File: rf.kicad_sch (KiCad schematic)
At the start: 10 parts, among them Q1 2N7002

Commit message: finish up everything but nfc
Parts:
- added U11: SN74AUP1G17, Package_TO_SOT_SMD:Diodes_SOT-553, symbol 74xGxx:74LVC1G17
- added U13: ST25R3916B-AQET, ST25R3916B-AQET:QFN-32_L5.0-W5.0-P0.50-TL-EP3.5, symbol ST25R3916B-AQET:ST25R3916B-AQET
- C33: LCSC Part (none) -> C1538
- C34: footprint (none) -> Capacitor_SMD:C_0402_1005Metric; LCSC Part (none) -> C15195
- L5: footprint (none) -> custom_footprints:Generic_Solder_Pads_2P; now left out of the parts list
- Q1: LCSC Part (none) -> C8545
- R41: footprint (none) -> Resistor_SMD:R_0402_1005Metric; LCSC Part (none) -> C25744
- R42: footprint (none) -> Resistor_SMD:R_0402_1005Metric; LCSC Part (none) -> C25741
- R43: footprint (none) -> Resistor_SMD:R_0603_1608Metric; LCSC Part (none) -> C21190
- R44: footprint (none) -> Resistor_SMD:R_0402_1005Metric; LCSC Part (none) -> C25792
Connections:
- net GND: now also U11.3 (GND)
- net RF_WAKE: now also U11.4; no longer D3.1 (K), R44.2
- net RF_MOD renamed RF_DAT
- new net: D3.1 (K), R44.2, U11.2
- new net +3V3: U11.5 (VCC)
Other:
- moved on the sheet: C33, C34, D2, L5, Q1, R41, R42, R43, R44

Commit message: progress
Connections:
- net +3V3: now also U13.1 (VDD_IO)
- net GND: now also U13.12 (GND_DR), U13.16 (GND_DR)
- net NFC_CS: now reaches U13.29 (BSS)
- net NFC_CLK: now reaches U13.30 (SCLK/SCL)
- net NFC_DO: now reaches U13.31 (MOSI)
- net NFC_DI: now reaches U13.32 (MISO/SDA)
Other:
- moved on the sheet: U13

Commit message: push changes before removing fuel gauge
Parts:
- L5: now in the parts list
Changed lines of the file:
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@@
 		(unit 1)
 		(exclude_from_sim no)
-		(in_bom no)
+		(in_bom yes)
 		(on_board yes)
 		(dnp no)

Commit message: hopefully final schematic before splitting out
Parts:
- added C40, C41, C60: 10pF, Capacitor_SMD:C_0402_1005Metric, symbol Device:C_Small
- added C42, C46, C47, C49, C51, C53: 2.2uF, Capacitor_SMD:C_0402_1005Metric, symbol Device:C_Small
- added C43: 22nF, Capacitor_SMD:C_0402_1005Metric, symbol Device:C_Small
- added C44, C45, C48, C50, C52, C54, C56: 10nF, Capacitor_SMD:C_0402_1005Metric, symbol Device:C_Small
- added C55: 1uF, Capacitor_SMD:C_0402_1005Metric, symbol Device:C_Small
- added C57: 680pF, Capacitor_SMD:C_0402_1005Metric, symbol Device:C_Small
- added C58: 58pF, Capacitor_SMD:C_0402_1005Metric, symbol Device:C_Small
- added C59: 3pF, Capacitor_SMD:C_0402_1005Metric, symbol Device:C_Small
- added C61: 220pF, Capacitor_SMD:C_0402_1005Metric, symbol Device:C_Small
- added L7: 1462360151, custom_footprints:Generic_Solder_Pads_2P, symbol Device:L
- added L8: 270nH, Inductor_SMD:L_0603_1608Metric, symbol Device:L_Small
- added R24: 5.8, Resistor_SMD:R_0402_1005Metric, symbol Device:R_Small
- added TP14: NFC_CSO, TestPoint:TestPoint_Pad_D1.0mm, symbol Connector:TestPoint
- added TP15: NFC_CSI, TestPoint:TestPoint_Pad_D1.0mm, symbol Connector:TestPoint
- added Y3: 27.12MHz, Crystal:Crystal_SMD_2016-4Pin_2.0x1.6mm, symbol Device:Crystal_GND24_Small
- L6: renamed from L5; now left out of the parts list
- renumbered C33 to C38, C34 to C39, R41 to R20, R44 to R21, R42 to R22, R43 to R23, U11 to U12
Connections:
- net +3V3: now also U13.10 (VDD_TX), U13.8 (VDD), C44.1, C51.1, C52.1, C53.1, C54.1
- net GND: now also U13.20 (I2C_EN), U13.21 (VSS), U13.26 (GND_A), U13.33 (EP), U13.6 (GND_D), C40.2, C41.2, C42.2, C43.2, C44.2, C45.2, C46.2, C47.2, C48.2, C49.2, C50.2, C51.2, C52.2, C53.2, C54.2, C55.2, C56.2, C57.2, C59.2, C61.2, L7.2, Y3.2, Y3.4
- net VDD_AM: now reaches U13.11 (VDD_AM)
- net VDD_AM: now also C42.1, C43.1
- net RFO1: now reaches U13.13 (RFO1)
- net RFO1: now also L8.1
- net VDD_RF: now reaches U13.14 (VDD_DR)
- net VDD_RF: now also U13.9 (VDD_RF), C47.1, C48.1
- net at U13.2 (CSO): now also TP14.1
- net RFI1: now reaches U13.22 (RFI1)
- net RFI1: now also C60.1, C61.1
- net at U13.24 (AGDC): now also C55.1, C56.1
- net at U13.25 (CSI): now also TP15.1
- net NFC_INT: now reaches U13.27 (IRQ)
- net VDD_D: now reaches U13.3 (VDD_D)
- net VDD_D: now also C45.1, C46.1
- net XTO: now reaches U13.4 (XTO)
- net XTO: now also C41.1, Y3.3
- net XTI: now reaches U13.5 (XTI)
- net XTI: now also C40.1, Y3.1
- net VDD_A: now reaches U13.7 (VDD_A)
- net VDD_A: now also C49.1, C50.1
- new net: C57.1, C58.1, L8.2
- new net: C58.2, C59.1, C60.2, R24.1
- new net: L7.1, R24.2
- no-connect marks 0 -> 6
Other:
- moved on the sheet: C38, C39, D2, D3, L6, Q1, R20, R21, R22, R23, U12, U13

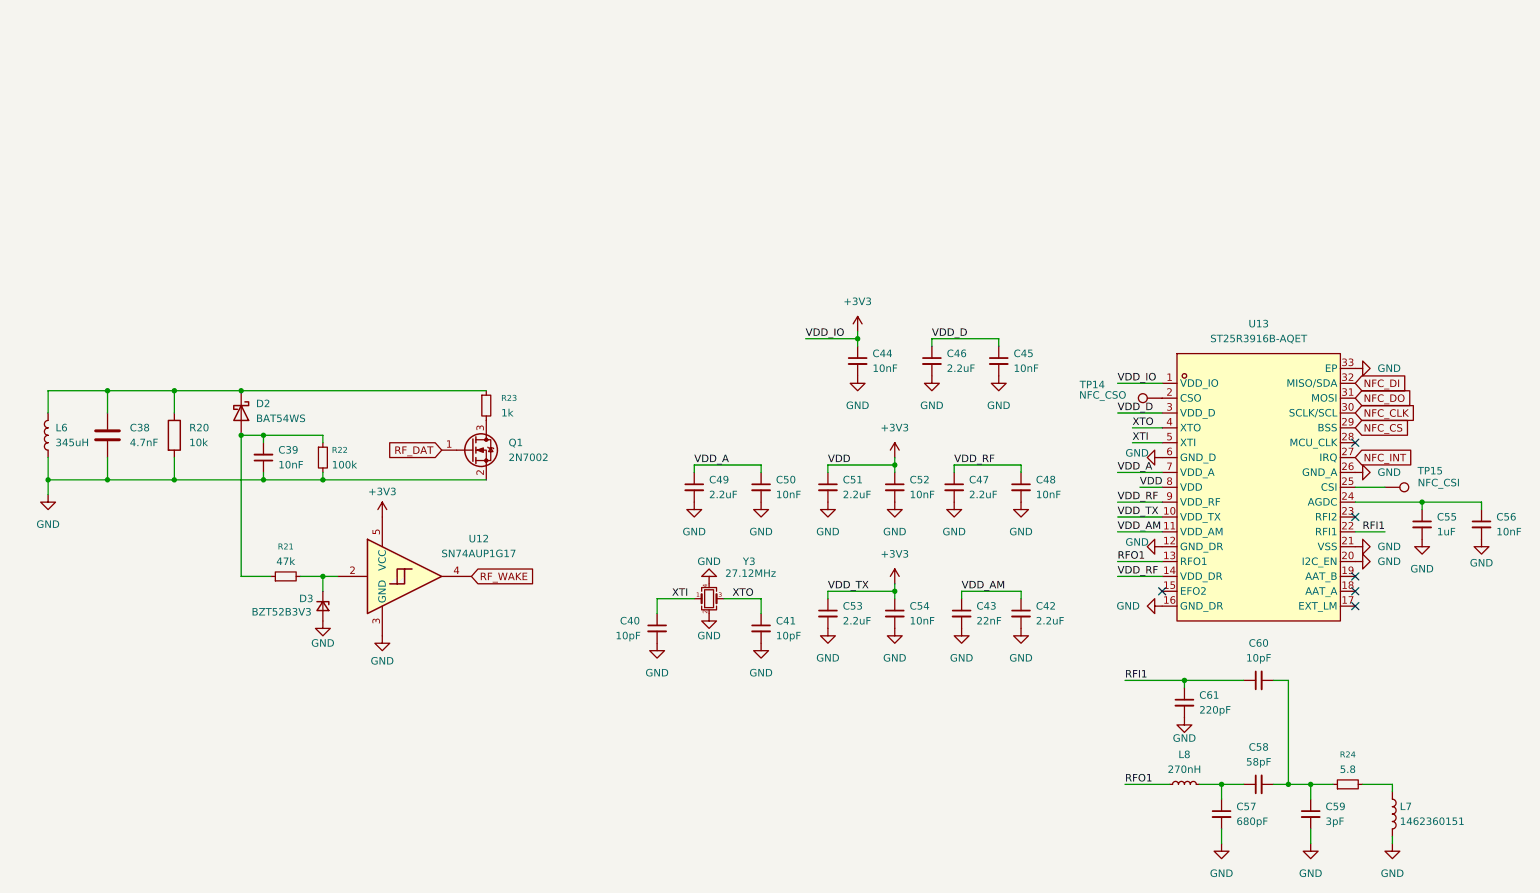
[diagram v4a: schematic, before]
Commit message: prepare schematic for devboard
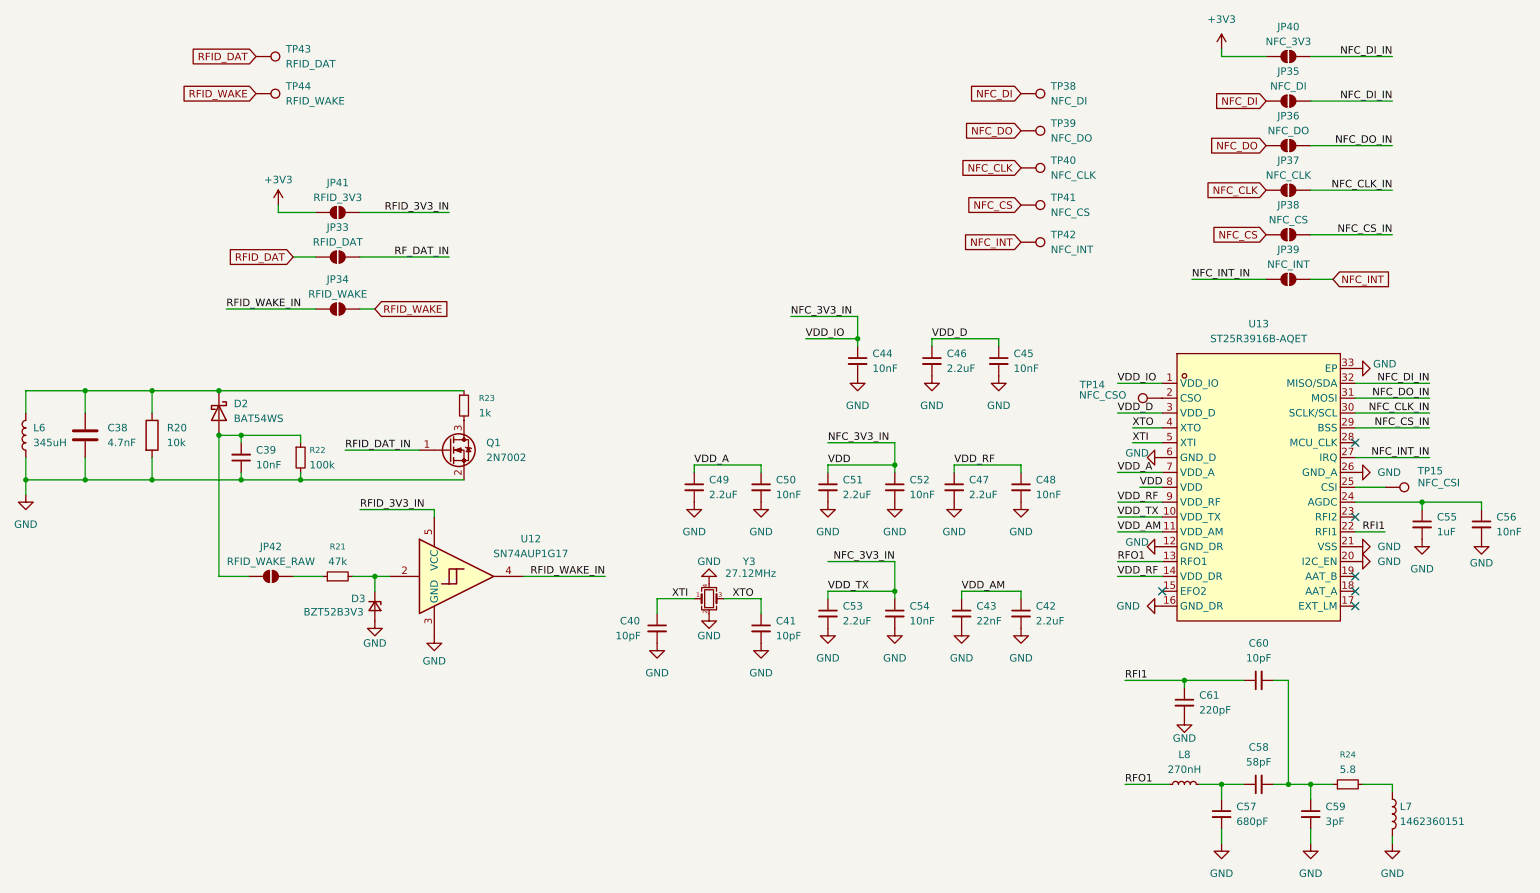
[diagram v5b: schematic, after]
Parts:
- added JP33: RFID_DAT, Jumper:SolderJumper-2_P1.3mm_Open_Pad1.0x1.5mm, symbol Jumper:SolderJumper_2_Open
- added JP34: RFID_WAKE, Jumper:SolderJumper-2_P1.3mm_Open_Pad1.0x1.5mm, symbol Jumper:SolderJumper_2_Open
- added JP35: NFC_DI, Jumper:SolderJumper-2_P1.3mm_Open_Pad1.0x1.5mm, symbol Jumper:SolderJumper_2_Open
- added JP36: NFC_DO, Jumper:SolderJumper-2_P1.3mm_Open_Pad1.0x1.5mm, symbol Jumper:SolderJumper_2_Open
- added JP37: NFC_CLK, Jumper:SolderJumper-2_P1.3mm_Open_Pad1.0x1.5mm, symbol Jumper:SolderJumper_2_Open
- added JP38: NFC_CS, Jumper:SolderJumper-2_P1.3mm_Open_Pad1.0x1.5mm, symbol Jumper:SolderJumper_2_Open
- added JP39: NFC_INT, Jumper:SolderJumper-2_P1.3mm_Open_Pad1.0x1.5mm, symbol Jumper:SolderJumper_2_Open
- added JP40: NFC_3V3, Jumper:SolderJumper-2_P1.3mm_Open_Pad1.0x1.5mm, symbol Jumper:SolderJumper_2_Open
- added JP41: RFID_3V3, Jumper:SolderJumper-2_P1.3mm_Open_Pad1.0x1.5mm, symbol Jumper:SolderJumper_2_Open
- added JP42: RFID_WAKE_RAW, Jumper:SolderJumper-2_P1.3mm_Open_Pad1.0x1.5mm, symbol Jumper:SolderJumper_2_Open
- added TP38: NFC_DI, TestPoint:TestPoint_Pad_D1.0mm, symbol Connector:TestPoint
- added TP39: NFC_DO, TestPoint:TestPoint_Pad_D1.0mm, symbol Connector:TestPoint
- added TP40: NFC_CLK, TestPoint:TestPoint_Pad_D1.0mm, symbol Connector:TestPoint
- added TP41: NFC_CS, TestPoint:TestPoint_Pad_D1.0mm, symbol Connector:TestPoint
- added TP42: NFC_INT, TestPoint:TestPoint_Pad_D1.0mm, symbol Connector:TestPoint
- added TP43: RFID_DAT, TestPoint:TestPoint_Pad_D1.0mm, symbol Connector:TestPoint
- added TP44: RFID_WAKE, TestPoint:TestPoint_Pad_D1.0mm, symbol Connector:TestPoint
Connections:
- net +3V3: now also JP40.1 (A), JP41.1 (A); no longer C44.1, C51.1, C52.1, C53.1, C54.1, U12.5 (VCC), U13.1 (VDD_IO), U13.10 (VDD_TX), U13.8 (VDD)
- net NFC_CLK: now also JP37.1 (A), TP40.1; no longer U13.30 (SCLK/SCL)
- net NFC_CS: now also JP38.1 (A), TP41.1; no longer U13.29 (BSS)
- net NFC_DI: now also JP35.1 (A), TP38.1; no longer U13.32 (MISO/SDA)
- net NFC_DO: now also JP36.1 (A), TP39.1; no longer U13.31 (MOSI)
- net NFC_INT: now also JP39.2 (B), TP42.1; no longer U13.27 (IRQ)
- net at C39.2, D2.2 (A), R22.1: now also JP42.1 (A); no longer R21.1
- net RF_DAT renamed RFID_DAT_IN
- net RF_WAKE renamed RFID_WAKE_IN
- net RFID_WAKE_IN: now also JP34.1 (A)
- new net: JP42.2 (B), R21.1
- new net NFC_3V3_IN: C44.1, C51.1, C52.1, C53.1, C54.1, U13.1 (VDD_IO), U13.10 (VDD_TX), U13.8 (VDD)
- new net NFC_CLK_IN: JP37.2 (B), U13.30 (SCLK/SCL)
- new net NFC_CS_IN: JP38.2 (B), U13.29 (BSS)
- new net NFC_DI_IN: JP35.2 (B), JP40.2 (B), U13.32 (MISO/SDA)
- new net NFC_DO_IN: JP36.2 (B), U13.31 (MOSI)
- new net NFC_INT_IN: JP39.1 (A), U13.27 (IRQ)
- new net RFID_3V3_IN: JP41.2 (B), U12.5 (VCC)
- new net RFID_DAT: JP33.1 (A), TP43.1
- new net RFID_WAKE: JP34.2 (B), TP44.1
- new net RF_DAT_IN: JP33.2 (B)
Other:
- moved on the sheet: C38, C39, D2, D3, L6, Q1, R20, R21, R22, R23, U12

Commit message: huge progress on bentoboard, schematic fixes
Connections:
- net RF_DAT_IN is gone; now on net RFID_DAT_IN: JP33.2 (B)
- net NFC_3V3_IN: now also JP40.2 (B)
- net NFC_DI_IN: no longer JP40.2 (B)
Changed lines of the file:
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@@
 		)
 	)
-	(label "NFC_DI_IN"
+	(label "NFC_3V3_IN"
 		(at 254 22.86 180)
 		(effects
@@
 		)
 	)
-	(label "RF_DAT_IN"
+	(label "RFID_DAT_IN"
 		(at 92.71 57.15 180)
 		(effects

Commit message: fixups before manufacturing pt1
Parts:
- R24: LCSC Part C423471 -> C423151
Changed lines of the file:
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@@
 			)
 		)
-		(property "LCSC Part" "C423471"
+		(property "LCSC Part" "C423151"
 			(at 246.38 147.32 90)
 			(effects

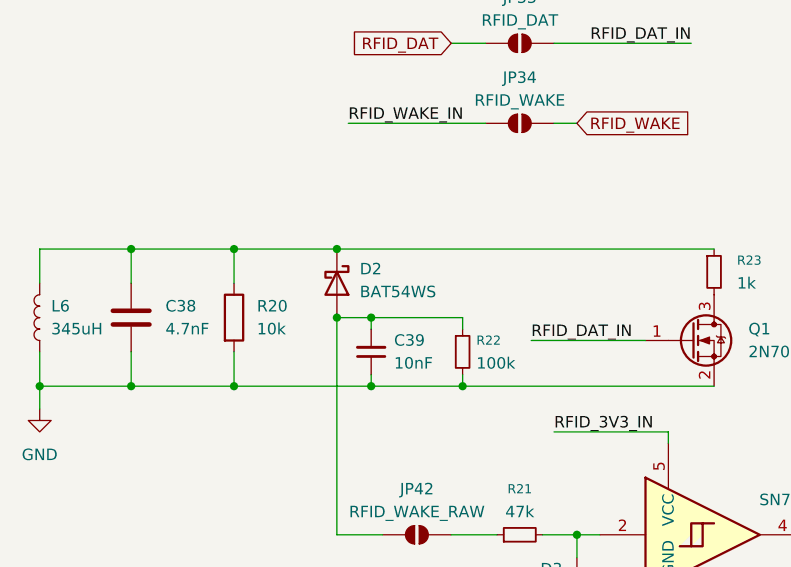
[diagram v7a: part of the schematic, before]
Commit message: oops fix: reversed diodes
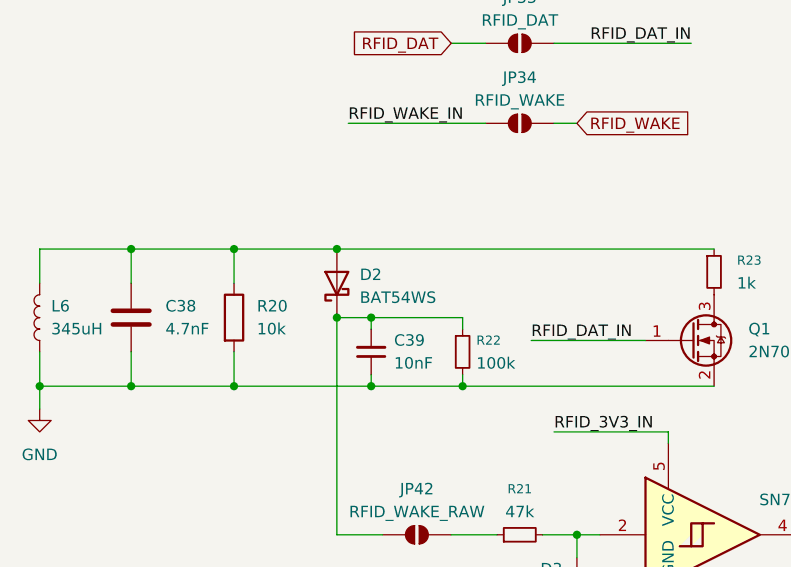
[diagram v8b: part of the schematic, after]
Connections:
- net at C38.1, L6.2, R20.1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: now also D2.2 (A); no longer D2.1 (K)
- net at C39.2, JP42.1 (A), R22.1: now also D2.1 (K); no longer D2.2 (A)
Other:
- moved on the sheet: D2
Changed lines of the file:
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@@
 	(symbol
 		(lib_id "Device:D_Schottky")
-		(at 53.34 83.82 270)
+		(at 53.34 83.82 90)
 		(unit 1)
 		(exclude_from_sim no)
@@
 		(fields_autoplaced yes)
 		(property "Reference" "D2"
-			(at 55.88 82.2324 90)
+			(at 55.88 82.8674 90)
 			(effects
 				(font
 					(size 1.27 1.27)
 				)
-				(justify left)
+				(justify right)
 			)
 		)
 		(property "Value" "BAT54WS"
-			(at 55.88 84.7724 90)
+			(at 55.88 85.4074 90)
 			(effects
 				(font
 					(size 1.27 1.27)
 				)
-				(justify left)
+				(justify right)
 			)
 		)
